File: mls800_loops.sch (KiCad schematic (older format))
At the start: 52 parts, among them J10 JACK_2P_STACK, J11 JACK_2P_SW, J2 JACK_2P_SW, J3 JACK_2P_STACK, J4 JACK_2P_STACK, J5 JACK_2P_STACK, J6 JACK_2P_STACK, J7 JACK_2P_STACK, J8 JACK_2P_STACK, J9 JACK_2P_STACK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

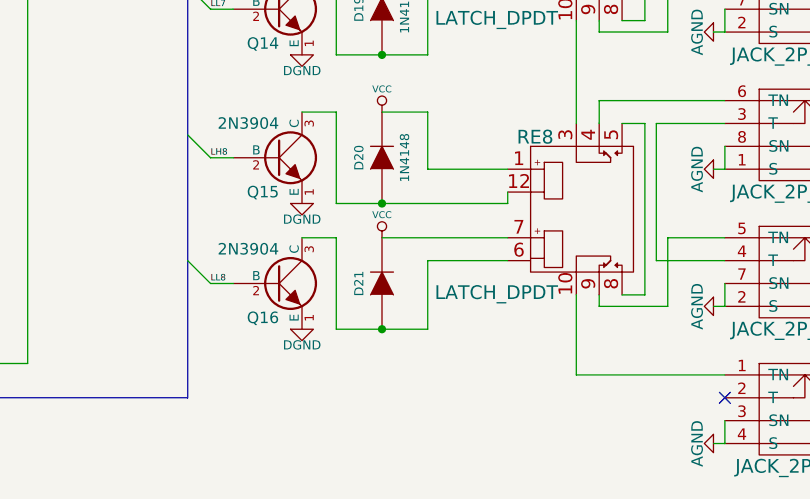
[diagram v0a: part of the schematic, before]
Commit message: MLS800
* footprint associations
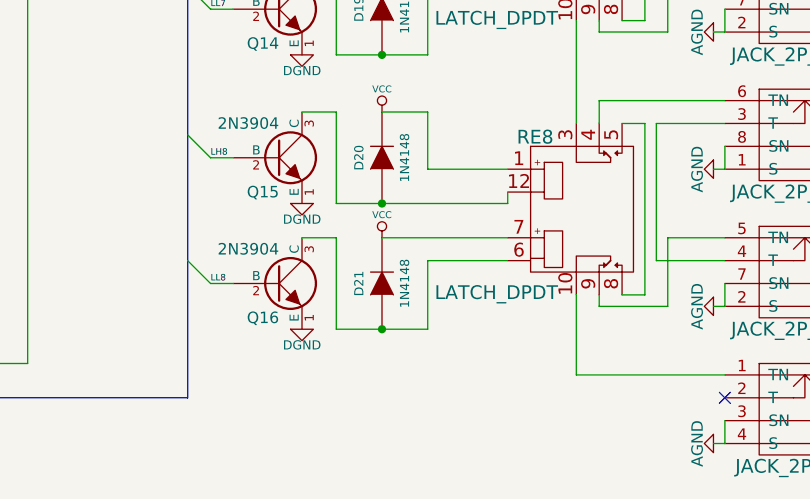
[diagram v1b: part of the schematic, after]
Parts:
- D21: value Imported:SOD-123 -> 1N4148; footprint ~ -> Imported:SOD-123
- Q1, Q10, Q11, Q12, Q13, Q14, Q15, Q16, Q2, Q3, Q4, Q5, Q6, Q7, Q8, Q9: footprint ~ -> Housings_SOT-23_SOT-143_TSOT-6:SOT23_Transistor_Handsoldering_RevB_14Mar2014
- R18: footprint ~ -> Resistors_SMD:R_0805_HandSoldering
- U4: footprint Housings_SSOP:SSOP-28 -> Housings_SSOP:SSOP-28_5.3x10.2mm_Pitch0.65mm
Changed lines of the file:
@@
 F 0 "U4" H 1500 3100 50  0000 C CNN
 F 1 "MCP23017" H 2500 900 50  0000 C CNN
-F 2 "Housings_SSOP:SSOP-28" H 1550 900 50  0001 C CNN
+F 2 "Housings_SSOP:SSOP-28_5.3x10.2mm_Pitch0.65mm" H 1550 900 50  0001 C CNN
 F 3 "DOCUMENTATION" H 2050 1950 50  0001 C CNN
 	1    2050 2000
@@
 F 0 "R18" V 930 1150 40  0000 C CNN
 F 1 "1k" V 857 1151 40  0000 C CNN
-F 2 "~" V 780 1150 30  0000 C CNN
+F 2 "Resistors_SMD:R_0805_HandSoldering" V 780 1150 30  0001 C CNN
 F 3 "~" H 850 1150 30  0000 C CNN
 	1    850  1150
@@
 F 0 "Q1" H 3900 1300 50  0000 R CNN
 F 1 "2N3904" H 3900 1600 50  0000 R CNN
-F 2 "~" H 3900 1450 60  0000 C CNN
+F 2 "Housings_SOT-23_SOT-143_TSOT-6:SOT23_Transistor_Handsoldering_RevB_14Mar2014" H 3900 1450 60  0001 C CNN
 F 3 "~" H 3900 1450 60  0000 C CNN
 	1    3900 1450
@@
 F 0 "Q2" H 3900 1850 50  0000 R CNN
 F 1 "2N3904" H 3900 2150 50  0000 R CNN
-F 2 "~" H 3900 2000 60  0000 C CNN
+F 2 "Housings_SOT-23_SOT-143_TSOT-6:SOT23_Transistor_Handsoldering_RevB_14Mar2014" H 3900 2000 60  0001 C CNN
 F 3 "~" H 3900 2000 60  0000 C CNN
 	1    3900 2000
@@
 F 0 "Q3" H 3900 2500 50  0000 R CNN
 F 1 "2N3904" H 3900 2800 50  0000 R CNN
-F 2 "~" H 3900 2650 60  0000 C CNN
+F 2 "Housings_SOT-23_SOT-143_TSOT-6:SOT23_Transistor_Handsoldering_RevB_14Mar2014" H 3900 2650 60  0001 C CNN
 F 3 "~" H 3900 2650 60  0000 C CNN
 	1    3900 2650
@@
 F 0 "Q4" H 3900 3050 50  0000 R CNN
 F 1 "2N3904" H 3900 3350 50  0000 R CNN
-F 2 "~" H 3900 3200 60  0000 C CNN
+F 2 "Housings_SOT-23_SOT-143_TSOT-6:SOT23_Transistor_Handsoldering_RevB_14Mar2014" H 3900 3200 60  0001 C CNN
 F 3 "~" H 3900 3200 60  0000 C CNN
 	1    3900 3200
@@
 F 0 "Q5" H 3900 3700 50  0000 R CNN
 F 1 "2N3904" H 3900 4000 50  0000 R CNN
-F 2 "~" H 3900 3850 60  0000 C CNN
+F 2 "Housings_SOT-23_SOT-143_TSOT-6:SOT23_Transistor_Handsoldering_RevB_14Mar2014" H 3900 3850 60  0001 C CNN
 F 3 "~" H 3900 3850 60  0000 C CNN
 	1    3900 3850
@@
 F 0 "Q6" H 3900 4250 50  0000 R CNN
 F 1 "2N3904" H 3900 4550 50  0000 R CNN
-F 2 "~" H 3900 4400 60  0000 C CNN
+F 2 "Housings_SOT-23_SOT-143_TSOT-6:SOT23_Transistor_Handsoldering_RevB_14Mar2014" H 3900 4400 60  0001 C CNN
 F 3 "~" H 3900 4400 60  0000 C CNN
 	1    3900 4400
@@
 F 0 "Q7" H 3900 4900 50  0000 R CNN
 F 1 "2N3904" H 3900 5200 50  0000 R CNN
-F 2 "~" H 3900 5050 60  0000 C CNN
+F 2 "Housings_SOT-23_SOT-143_TSOT-6:SOT23_Transistor_Handsoldering_RevB_14Mar2014" H 3900 5050 60  0001 C CNN
 F 3 "~" H 3900 5050 60  0000 C CNN
 	1    3900 5050
@@
 F 0 "Q8" H 3900 5450 50  0000 R CNN
 F 1 "2N3904" H 3900 5750 50  0000 R CNN
-F 2 "~" H 3900 5600 60  0000 C CNN
+F 2 "Housings_SOT-23_SOT-143_TSOT-6:SOT23_Transistor_Handsoldering_RevB_14Mar2014" H 3900 5600 60  0001 C CNN
 F 3 "~" H 3900 5600 60  0000 C CNN
 	1    3900 5600
@@
 F 0 "Q9" H 8200 1300 50  0000 R CNN
 F 1 "2N3904" H 8200 1600 50  0000 R CNN
-F 2 "~" H 8200 1450 60  0000 C CNN
+F 2 "Housings_SOT-23_SOT-143_TSOT-6:SOT23_Transistor_Handsoldering_RevB_14Mar2014" H 8200 1450 60  0001 C CNN
 F 3 "~" H 8200 1450 60  0000 C CNN
 	1    8200 1450
@@
 F 0 "Q10" H 8200 1850 50  0000 R CNN
 F 1 "2N3904" H 8200 2150 50  0000 R CNN
-F 2 "~" H 8200 2000 60  0000 C CNN
+F 2 "Housings_SOT-23_SOT-143_TSOT-6:SOT23_Transistor_Handsoldering_RevB_14Mar2014" H 8200 2000 60  0001 C CNN
 F 3 "~" H 8200 2000 60  0000 C CNN
 	1    8200 2000
@@
 F 0 "Q11" H 8200 2500 50  0000 R CNN
 F 1 "2N3904" H 8200 2800 50  0000 R CNN
-F 2 "~" H 8200 2650 60  0000 C CNN
+F 2 "Housings_SOT-23_SOT-143_TSOT-6:SOT23_Transistor_Handsoldering_RevB_14Mar2014" H 8200 2650 60  0001 C CNN
 F 3 "~" H 8200 2650 60  0000 C CNN
 	1    8200 2650
@@
 F 0 "Q12" H 8200 3050 50  0000 R CNN
 F 1 "2N3904" H 8200 3350 50  0000 R CNN
-F 2 "~" H 8200 3200 60  0000 C CNN
+F 2 "Housings_SOT-23_SOT-143_TSOT-6:SOT23_Transistor_Handsoldering_RevB_14Mar2014" H 8200 3200 60  0001 C CNN
 F 3 "~" H 8200 3200 60  0000 C CNN
 	1    8200 3200
@@
 F 0 "Q13" H 8200 3700 50  0000 R CNN
 F 1 "2N3904" H 8200 4000 50  0000 R CNN
-F 2 "~" H 8200 3850 60  0000 C CNN
+F 2 "Housings_SOT-23_SOT-143_TSOT-6:SOT23_Transistor_Handsoldering_RevB_14Mar2014" H 8200 3850 60  0001 C CNN
 F 3 "~" H 8200 3850 60  0000 C CNN
 	1    8200 3850
@@
 F 0 "Q14" H 8200 4250 50  0000 R CNN
 F 1 "2N3904" H 8200 4550 50  0000 R CNN
-F 2 "~" H 8200 4400 60  0000 C CNN
+F 2 "Housings_SOT-23_SOT-143_TSOT-6:SOT23_Transistor_Handsoldering_RevB_14Mar2014" H 8200 4400 60  0001 C CNN
 F 3 "~" H 8200 4400 60  0000 C CNN
 	1    8200 4400
@@
 F 0 "Q15" H 8200 4900 50  0000 R CNN
 F 1 "2N3904" H 8200 5200 50  0000 R CNN
-F 2 "~" H 8200 5050 60  0000 C CNN
+F 2 "Housings_SOT-23_SOT-143_TSOT-6:SOT23_Transistor_Handsoldering_RevB_14Mar2014" H 8200 5050 60  0001 C CNN
 F 3 "~" H 8200 5050 60  0000 C CNN
 	1    8200 5050
@@
 F 0 "Q16" H 8200 5450 50  0000 R CNN
 F 1 "2N3904" H 8200 5750 50  0000 R CNN
-F 2 "~" H 8200 5600 60  0000 C CNN
+F 2 "Housings_SOT-23_SOT-143_TSOT-6:SOT23_Transistor_Handsoldering_RevB_14Mar2014" H 8200 5600 60  0001 C CNN
 F 3 "~" H 8200 5600 60  0000 C CNN
 	1    8200 5600
@@
 P 8650 5600
 F 0 "D21" H 8650 5700 40  0000 C CNN
-F 1 "Imported:SOD-123" H 8650 5500 40  0001 C CNN
-F 2 "~" H 8650 5600 60  0000 C CNN
+F 1 "1N4148" H 8650 5500 40  0000 C CNN
+F 2 "Imported:SOD-123" H 8650 5600 60  0001 C CNN
 F 3 "~" H 8650 5600 60  0000 C CNN
 	1    8650 5600

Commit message: MLS800
* added two news footprints (bistable relay & simple neutrik jack)
* footprint associations
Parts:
- J10, J3, J4, J5, J6, J7, J8, J9: footprint ~ -> (none)
- J11, J2: footprint ~ -> Custom-conn:NRJ4HF-1
- RE1, RE2, RE3, RE4, RE5, RE6, RE7, RE8: footprint ~ -> Custom-device:Relay_SMD_DPDT-RT2_bistabil
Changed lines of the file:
@@
 F 0 "RE1" H 5020 2040 60  0000 C CNN
 F 1 "LATCH_DPDT" H 4850 1360 60  0000 C CNN
-F 2 "~" H 5480 1700 60  0000 C CNN
+F 2 "Custom-device:Relay_SMD_DPDT-RT2_bistabil" H 5480 1700 60  0001 C CNN
 F 3 "~" H 5480 1700 60  0000 C CNN
 	1    5250 1700
@@
 F 0 "J3" H 5950 1100 60  0000 C CNN
 F 1 "JACK_2P_STACK" H 6400 1600 60  0000 C CNN
-F 2 "~" H 6300 1350 60  0000 C CNN
+F 2 "" H 6300 1350 60  0001 C CNN
 F 3 "~" H 6300 1350 60  0000 C CNN
 	1    6300 1350
@@
 F 0 "J3" H 5950 1700 60  0000 C CNN
 F 1 "JACK_2P_STACK" H 6400 2200 60  0000 C CNN
-F 2 "~" H 6300 1950 60  0000 C CNN
+F 2 "" H 6300 1950 60  0001 C CNN
 F 3 "~" H 6300 1950 60  0000 C CNN
 	2    6300 1950
@@
 F 0 "J2" H 5950 500 60  0000 C CNN
 F 1 "JACK_2P_SW" H 6450 1000 60  0000 C CNN
-F 2 "~" H 6300 750 60  0000 C CNN
+F 2 "Custom-conn:NRJ4HF-1" H 6300 750 60  0001 C CNN
 F 3 "~" H 6300 750 60  0000 C CNN
 	1    6300 750
@@
 F 0 "RE2" H 5020 3240 60  0000 C CNN
 F 1 "LATCH_DPDT" H 4850 2560 60  0000 C CNN
-F 2 "~" H 5480 2900 60  0000 C CNN
+F 2 "Custom-device:Relay_SMD_DPDT-RT2_bistabil" H 5480 2900 60  0001 C CNN
 F 3 "~" H 5480 2900 60  0000 C CNN
 	1    5250 2900
@@
 F 0 "J4" H 5950 2300 60  0000 C CNN
 F 1 "JACK_2P_STACK" H 6400 2800 60  0000 C CNN
-F 2 "~" H 6300 2550 60  0000 C CNN
+F 2 "" H 6300 2550 60  0001 C CNN
 F 3 "~" H 6300 2550 60  0000 C CNN
 	1    6300 2550
@@
 F 0 "J4" H 5950 2900 60  0000 C CNN
 F 1 "JACK_2P_STACK" H 6400 3400 60  0000 C CNN
-F 2 "~" H 6300 3150 60  0000 C CNN
+F 2 "" H 6300 3150 60  0001 C CNN
 F 3 "~" H 6300 3150 60  0000 C CNN
 	2    6300 3150
@@
 F 0 "RE3" H 5020 4440 60  0000 C CNN
 F 1 "LATCH_DPDT" H 4850 3760 60  0000 C CNN
-F 2 "~" H 5480 4100 60  0000 C CNN
+F 2 "Custom-device:Relay_SMD_DPDT-RT2_bistabil" H 5480 4100 60  0001 C CNN
 F 3 "~" H 5480 4100 60  0000 C CNN
 	1    5250 4100
@@
 F 0 "J5" H 5950 3500 60  0000 C CNN
 F 1 "JACK_2P_STACK" H 6400 4000 60  0000 C CNN
-F 2 "~" H 6300 3750 60  0000 C CNN
+F 2 "" H 6300 3750 60  0001 C CNN
 F 3 "~" H 6300 3750 60  0000 C CNN
 	1    6300 3750
@@
 F 0 "J5" H 5950 4100 60  0000 C CNN
 F 1 "JACK_2P_STACK" H 6400 4600 60  0000 C CNN
-F 2 "~" H 6300 4350 60  0000 C CNN
+F 2 "" H 6300 4350 60  0001 C CNN
 F 3 "~" H 6300 4350 60  0000 C CNN
 	2    6300 4350
@@
 F 0 "RE4" H 5020 5640 60  0000 C CNN
 F 1 "LATCH_DPDT" H 4850 4960 60  0000 C CNN
-F 2 "~" H 5480 5300 60  0000 C CNN
+F 2 "Custom-device:Relay_SMD_DPDT-RT2_bistabil" H 5480 5300 60  0001 C CNN
 F 3 "~" H 5480 5300 60  0000 C CNN
 	1    5250 5300
@@
 F 0 "J6" H 5950 4700 60  0000 C CNN
 F 1 "JACK_2P_STACK" H 6400 5200 60  0000 C CNN
-F 2 "~" H 6300 4950 60  0000 C CNN
+F 2 "" H 6300 4950 60  0001 C CNN
 F 3 "~" H 6300 4950 60  0000 C CNN
 	1    6300 4950
@@
 F 0 "J6" H 5950 5300 60  0000 C CNN
 F 1 "JACK_2P_STACK" H 6400 5800 60  0000 C CNN
-F 2 "~" H 6300 5550 60  0000 C CNN
+F 2 "" H 6300 5550 60  0001 C CNN
 F 3 "~" H 6300 5550 60  0000 C CNN
 	2    6300 5550
@@
 F 0 "RE5" H 9320 2040 60  0000 C CNN
 F 1 "LATCH_DPDT" H 9150 1360 60  0000 C CNN
-F 2 "~" H 9780 1700 60  0000 C CNN
+F 2 "Custom-device:Relay_SMD_DPDT-RT2_bistabil" H 9780 1700 60  0001 C CNN
 F 3 "~" H 9780 1700 60  0000 C CNN
 	1    9550 1700
@@
 F 0 "J7" H 10250 1100 60  0000 C CNN
 F 1 "JACK_2P_STACK" H 10700 1600 60  0000 C CNN
-F 2 "~" H 10600 1350 60  0000 C CNN
+F 2 "" H 10600 1350 60  0001 C CNN
 F 3 "~" H 10600 1350 60  0000 C CNN
 	1    10600 1350
@@
 F 0 "J7" H 10250 1700 60  0000 C CNN
 F 1 "JACK_2P_STACK" H 10700 2200 60  0000 C CNN
-F 2 "~" H 10600 1950 60  0000 C CNN
+F 2 "" H 10600 1950 60  0001 C CNN
 F 3 "~" H 10600 1950 60  0000 C CNN
 	2    10600 1950
@@
 F 0 "RE6" H 9320 3240 60  0000 C CNN
 F 1 "LATCH_DPDT" H 9150 2560 60  0000 C CNN
-F 2 "~" H 9780 2900 60  0000 C CNN
+F 2 "Custom-device:Relay_SMD_DPDT-RT2_bistabil" H 9780 2900 60  0001 C CNN
 F 3 "~" H 9780 2900 60  0000 C CNN
 	1    9550 2900
@@
 F 0 "J8" H 10250 2300 60  0000 C CNN
 F 1 "JACK_2P_STACK" H 10700 2800 60  0000 C CNN
-F 2 "~" H 10600 2550 60  0000 C CNN
+F 2 "" H 10600 2550 60  0001 C CNN
 F 3 "~" H 10600 2550 60  0000 C CNN
 	1    10600 2550
@@
 F 0 "J8" H 10250 2900 60  0000 C CNN
 F 1 "JACK_2P_STACK" H 10700 3400 60  0000 C CNN
-F 2 "~" H 10600 3150 60  0000 C CNN
+F 2 "" H 10600 3150 60  0001 C CNN
 F 3 "~" H 10600 3150 60  0000 C CNN
 	2    10600 3150
@@
 F 0 "RE7" H 9320 4440 60  0000 C CNN
 F 1 "LATCH_DPDT" H 9150 3760 60  0000 C CNN
-F 2 "~" H 9780 4100 60  0000 C CNN
+F 2 "Custom-device:Relay_SMD_DPDT-RT2_bistabil" H 9780 4100 60  0001 C CNN
 F 3 "~" H 9780 4100 60  0000 C CNN
 	1    9550 4100
@@
 F 0 "J9" H 10250 3500 60  0000 C CNN
 F 1 "JACK_2P_STACK" H 10700 4000 60  0000 C CNN
-F 2 "~" H 10600 3750 60  0000 C CNN
+F 2 "" H 10600 3750 60  0001 C CNN
 F 3 "~" H 10600 3750 60  0000 C CNN
 	1    10600 3750
@@
 F 0 "J9" H 10250 4100 60  0000 C CNN
 F 1 "JACK_2P_STACK" H 10700 4600 60  0000 C CNN
-F 2 "~" H 10600 4350 60  0000 C CNN
+F 2 "" H 10600 4350 60  0001 C CNN
 F 3 "~" H 10600 4350 60  0000 C CNN
 	2    10600 4350
@@
 F 0 "RE8" H 9320 5640 60  0000 C CNN
 F 1 "LATCH_DPDT" H 9150 4960 60  0000 C CNN
-F 2 "~" H 9780 5300 60  0000 C CNN
+F 2 "Custom-device:Relay_SMD_DPDT-RT2_bistabil" H 9780 5300 60  0001 C CNN
 F 3 "~" H 9780 5300 60  0000 C CNN
 	1    9550 5300
@@
 F 0 "J10" H 10250 4700 60  0000 C CNN
 F 1 "JACK_2P_STACK" H 10700 5200 60  0000 C CNN
-F 2 "~" H 10600 4950 60  0000 C CNN
+F 2 "" H 10600 4950 60  0001 C CNN
 F 3 "~" H 10600 4950 60  0000 C CNN
 	1    10600 4950
@@
 F 0 "J10" H 10250 5300 60  0000 C CNN
 F 1 "JACK_2P_STACK" H 10700 5800 60  0000 C CNN
-F 2 "~" H 10600 5550 60  0000 C CNN
+F 2 "" H 10600 5550 60  0001 C CNN
 F 3 "~" H 10600 5550 60  0000 C CNN
 	2    10600 5550
@@
 F 0 "J11" H 10250 5900 60  0000 C CNN
 F 1 "JACK_2P_SW" H 10750 6400 60  0000 C CNN
-F 2 "~" H 10600 6150 60  0000 C CNN
+F 2 "Custom-conn:NRJ4HF-1" H 10600 6150 60  0001 C CNN
 F 3 "~" H 10600 6150 60  0000 C CNN
 	1    10600 6150

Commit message: MLS800
* added footprint for double jack
* footprints assignements
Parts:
- J10, J3, J4, J5, J6, J7, J8, J9: footprint (none) -> Custom-conn:NSJ8HL
- J11: footprint Custom-conn:NRJ4HF-1 -> Custom-conn:NSJ8HL
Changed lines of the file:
@@
 F 0 "J3" H 5950 1100 60  0000 C CNN
 F 1 "JACK_2P_STACK" H 6400 1600 60  0000 C CNN
-F 2 "" H 6300 1350 60  0001 C CNN
+F 2 "Custom-conn:NSJ8HL" H 6300 1350 60  0001 C CNN
 F 3 "~" H 6300 1350 60  0000 C CNN
 	1    6300 1350
@@
 F 0 "J3" H 5950 1700 60  0000 C CNN
 F 1 "JACK_2P_STACK" H 6400 2200 60  0000 C CNN
-F 2 "" H 6300 1950 60  0001 C CNN
+F 2 "Custom-conn:NSJ8HL" H 6300 1950 60  0001 C CNN
 F 3 "~" H 6300 1950 60  0000 C CNN
 	2    6300 1950
@@
 F 0 "J4" H 5950 2300 60  0000 C CNN
 F 1 "JACK_2P_STACK" H 6400 2800 60  0000 C CNN
-F 2 "" H 6300 2550 60  0001 C CNN
+F 2 "Custom-conn:NSJ8HL" H 6300 2550 60  0001 C CNN
 F 3 "~" H 6300 2550 60  0000 C CNN
 	1    6300 2550
@@
 F 0 "J4" H 5950 2900 60  0000 C CNN
 F 1 "JACK_2P_STACK" H 6400 3400 60  0000 C CNN
-F 2 "" H 6300 3150 60  0001 C CNN
+F 2 "Custom-conn:NSJ8HL" H 6300 3150 60  0001 C CNN
 F 3 "~" H 6300 3150 60  0000 C CNN
 	2    6300 3150
@@
 F 0 "J5" H 5950 3500 60  0000 C CNN
 F 1 "JACK_2P_STACK" H 6400 4000 60  0000 C CNN
-F 2 "" H 6300 3750 60  0001 C CNN
+F 2 "Custom-conn:NSJ8HL" H 6300 3750 60  0001 C CNN
 F 3 "~" H 6300 3750 60  0000 C CNN
 	1    6300 3750
@@
 F 0 "J5" H 5950 4100 60  0000 C CNN
 F 1 "JACK_2P_STACK" H 6400 4600 60  0000 C CNN
-F 2 "" H 6300 4350 60  0001 C CNN
+F 2 "Custom-conn:NSJ8HL" H 6300 4350 60  0001 C CNN
 F 3 "~" H 6300 4350 60  0000 C CNN
 	2    6300 4350
@@
 F 0 "J6" H 5950 4700 60  0000 C CNN
 F 1 "JACK_2P_STACK" H 6400 5200 60  0000 C CNN
-F 2 "" H 6300 4950 60  0001 C CNN
+F 2 "Custom-conn:NSJ8HL" H 6300 4950 60  0001 C CNN
 F 3 "~" H 6300 4950 60  0000 C CNN
 	1    6300 4950
@@
 F 0 "J6" H 5950 5300 60  0000 C CNN
 F 1 "JACK_2P_STACK" H 6400 5800 60  0000 C CNN
-F 2 "" H 6300 5550 60  0001 C CNN
+F 2 "Custom-conn:NSJ8HL" H 6300 5550 60  0001 C CNN
 F 3 "~" H 6300 5550 60  0000 C CNN
 	2    6300 5550
@@
 F 0 "J7" H 10250 1100 60  0000 C CNN
 F 1 "JACK_2P_STACK" H 10700 1600 60  0000 C CNN
-F 2 "" H 10600 1350 60  0001 C CNN
+F 2 "Custom-conn:NSJ8HL" H 10600 1350 60  0001 C CNN
 F 3 "~" H 10600 1350 60  0000 C CNN
 	1    10600 1350
@@
 F 0 "J7" H 10250 1700 60  0000 C CNN
 F 1 "JACK_2P_STACK" H 10700 2200 60  0000 C CNN
-F 2 "" H 10600 1950 60  0001 C CNN
+F 2 "Custom-conn:NSJ8HL" H 10600 1950 60  0001 C CNN
 F 3 "~" H 10600 1950 60  0000 C CNN
 	2    10600 1950
@@
 F 0 "J8" H 10250 2300 60  0000 C CNN
 F 1 "JACK_2P_STACK" H 10700 2800 60  0000 C CNN
-F 2 "" H 10600 2550 60  0001 C CNN
+F 2 "Custom-conn:NSJ8HL" H 10600 2550 60  0001 C CNN
 F 3 "~" H 10600 2550 60  0000 C CNN
 	1    10600 2550
@@
 F 0 "J8" H 10250 2900 60  0000 C CNN
 F 1 "JACK_2P_STACK" H 10700 3400 60  0000 C CNN
-F 2 "" H 10600 3150 60  0001 C CNN
+F 2 "Custom-conn:NSJ8HL" H 10600 3150 60  0001 C CNN
 F 3 "~" H 10600 3150 60  0000 C CNN
 	2    10600 3150
@@
 F 0 "J9" H 10250 3500 60  0000 C CNN
 F 1 "JACK_2P_STACK" H 10700 4000 60  0000 C CNN
-F 2 "" H 10600 3750 60  0001 C CNN
+F 2 "Custom-conn:NSJ8HL" H 10600 3750 60  0001 C CNN
 F 3 "~" H 10600 3750 60  0000 C CNN
 	1    10600 3750
@@
 F 0 "J9" H 10250 4100 60  0000 C CNN
 F 1 "JACK_2P_STACK" H 10700 4600 60  0000 C CNN
-F 2 "" H 10600 4350 60  0001 C CNN
+F 2 "Custom-conn:NSJ8HL" H 10600 4350 60  0001 C CNN
 F 3 "~" H 10600 4350 60  0000 C CNN
 	2    10600 4350
@@
 F 0 "J10" H 10250 4700 60  0000 C CNN
 F 1 "JACK_2P_STACK" H 10700 5200 60  0000 C CNN
-F 2 "" H 10600 4950 60  0001 C CNN
+F 2 "Custom-conn:NSJ8HL" H 10600 4950 60  0001 C CNN
 F 3 "~" H 10600 4950 60  0000 C CNN
 	1    10600 4950
@@
 F 0 "J10" H 10250 5300 60  0000 C CNN
 F 1 "JACK_2P_STACK" H 10700 5800 60  0000 C CNN
-F 2 "" H 10600 5550 60  0001 C CNN
+F 2 "Custom-conn:NSJ8HL" H 10600 5550 60  0001 C CNN
 F 3 "~" H 10600 5550 60  0000 C CNN
 	2    10600 5550
@@
 F 0 "J11" H 10250 5900 60  0000 C CNN
 F 1 "JACK_2P_SW" H 10750 6400 60  0000 C CNN
-F 2 "Custom-conn:NRJ4HF-1" H 10600 6150 60  0001 C CNN
+F 2 "Custom-conn:NSJ8HL" H 10600 6150 60  0001 C CNN
 F 3 "~" H 10600 6150 60  0000 C CNN
 	1    10600 6150

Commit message: MLS800
* fixed bistable relay pinout
* fixed lm340 pinout
* fixed missing footprints from older kicad version
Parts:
- J11: footprint Custom-conn:NSJ8HL -> Custom-conn:NRJ4HF-1
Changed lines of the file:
@@
 LIBS:custom-display
 LIBS:custom-micro
+LIBS:custom-regul
 LIBS:mls800-cache
 EELAYER 25 0
@@
 F 0 "J11" H 10250 5900 60  0000 C CNN
 F 1 "JACK_2P_SW" H 10750 6400 60  0000 C CNN
-F 2 "Custom-conn:NSJ8HL" H 10600 6150 60  0001 C CNN
+F 2 "Custom-conn:NRJ4HF-1" H 10600 6150 60  0001 C CNN
 F 3 "~" H 10600 6150 60  0000 C CNN
 	1    10600 6150

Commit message: MLS800
* routing
* reversed LL side of the MCP23017 loops control for better layout (needs to be impacted on code side)
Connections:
- net LL1: now also U4.8 (GPB7); no longer U4.1 (GPB0)
- net LL2: now also U4.7 (GPB6); no longer U4.2 (GPB1)
- net LL3: now also U4.6 (GPB5); no longer U4.3 (GPB2)
- net LL4: now also U4.5 (GPB4); no longer U4.4 (GPB3)
- net LL5: now also U4.4 (GPB3); no longer U4.5 (GPB4)
- net LL6: now also U4.3 (GPB2); no longer U4.6 (GPB5)
- net LL7: now also U4.2 (GPB1); no longer U4.7 (GPB6)
- net LL8: now also U4.1 (GPB0); no longer U4.8 (GPB7)
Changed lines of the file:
@@
 LH8
 Text Label 3000 1950 0    28   ~ 0
+LL8
+Text Label 3000 2050 0    28   ~ 0
+LL7
+Text Label 3000 2150 0    28   ~ 0
+LL6
+Text Label 3000 2250 0    28   ~ 0
+LL5
+Text Label 3000 2350 0    28   ~ 0
+LL4
+Text Label 3000 2450 0    28   ~ 0
+LL3
+Text Label 3000 2550 0    28   ~ 0
+LL2
+Text Label 3000 2650 0    28   ~ 0
 LL1
-Text Label 3000 2050 0    28   ~ 0
-LL2
-Text Label 3000 2150 0    28   ~ 0
-LL3
-Text Label 3000 2250 0    28   ~ 0
-LL4
-Text Label 3000 2350 0    28   ~ 0
-LL5
-Text Label 3000 2450 0    28   ~ 0
-LL6
-Text Label 3000 2550 0    28   ~ 0
-LL7
-Text Label 3000 2650 0    28   ~ 0
-LL8
 Text Notes 850  5850 0    197  ~ 39
 LOOPS
